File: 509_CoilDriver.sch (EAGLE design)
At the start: 230 parts, among them CN1 DF11-4DP-2DSA, CN10 826646-4, CN11 826646-4, CN12 BNC_ANGLE, CN13 BNC_ANGLE, CN14 BNC_ANGLE, CN15 DF11-4DP-2DSA, CN16 PCS-XE50LFD, CN17 PCS-XE50LFD, CN18 PH-2X5S, CN19 PIN_HEADER_SOCKET_14PIN, CN2 DF11-4DP-2DSA, CN20 DF11-14DP-2DSA, CN3 DF11-4DP-2DSA, CN4 DF11-4DP-2DSA, CN5 DF11-4DP-2DSA, CN6 DF11-4DP-2DSA, CN7 DF11-14DP-2DSA, CN8 PH-2X4S, CN9 DF11-4DP-2DSA, M1 VAB-3-10, M2 VAB-3-10, M3 VAB-3-10, SW1 A-12AV, SW2 A-12AV, SW3 A-12AV, SW4 A-12AV, U1 OPA2344EA, U10 74VHC4052AFT, U11 AD8227ARZ, U12 MAX4617CUE+, U13 MAX4617CUE+, U14 MAX4617CUE+, U15 MAX4617CUE+, U16 MAX4617CUE+, U17 MAX4617CUE+, U18 MAX4617CUE+, U19 MAX4617CUE+, U2 OPA2344EA, U20 MAX4617CUE+, U21 MAX4617CUE+, U22 MAX4617CUE+, U23 MAX4617CUE+, U24 MAX4617CUE+, U25 MAX4617CUE+, U26 TPS79933DDC, U27 5M160ZT100, U28 TPS79918DDC, U29 74VHC9541FT, U3 TS5A23159DGS, U30 TLP291GR, U4 TPS79933DDC, U5 OPA2344EA, U6 TPS3808G01DBV, U7 NJU7108F3, U8 OPA2344EA, U9 TS5A23159DGS

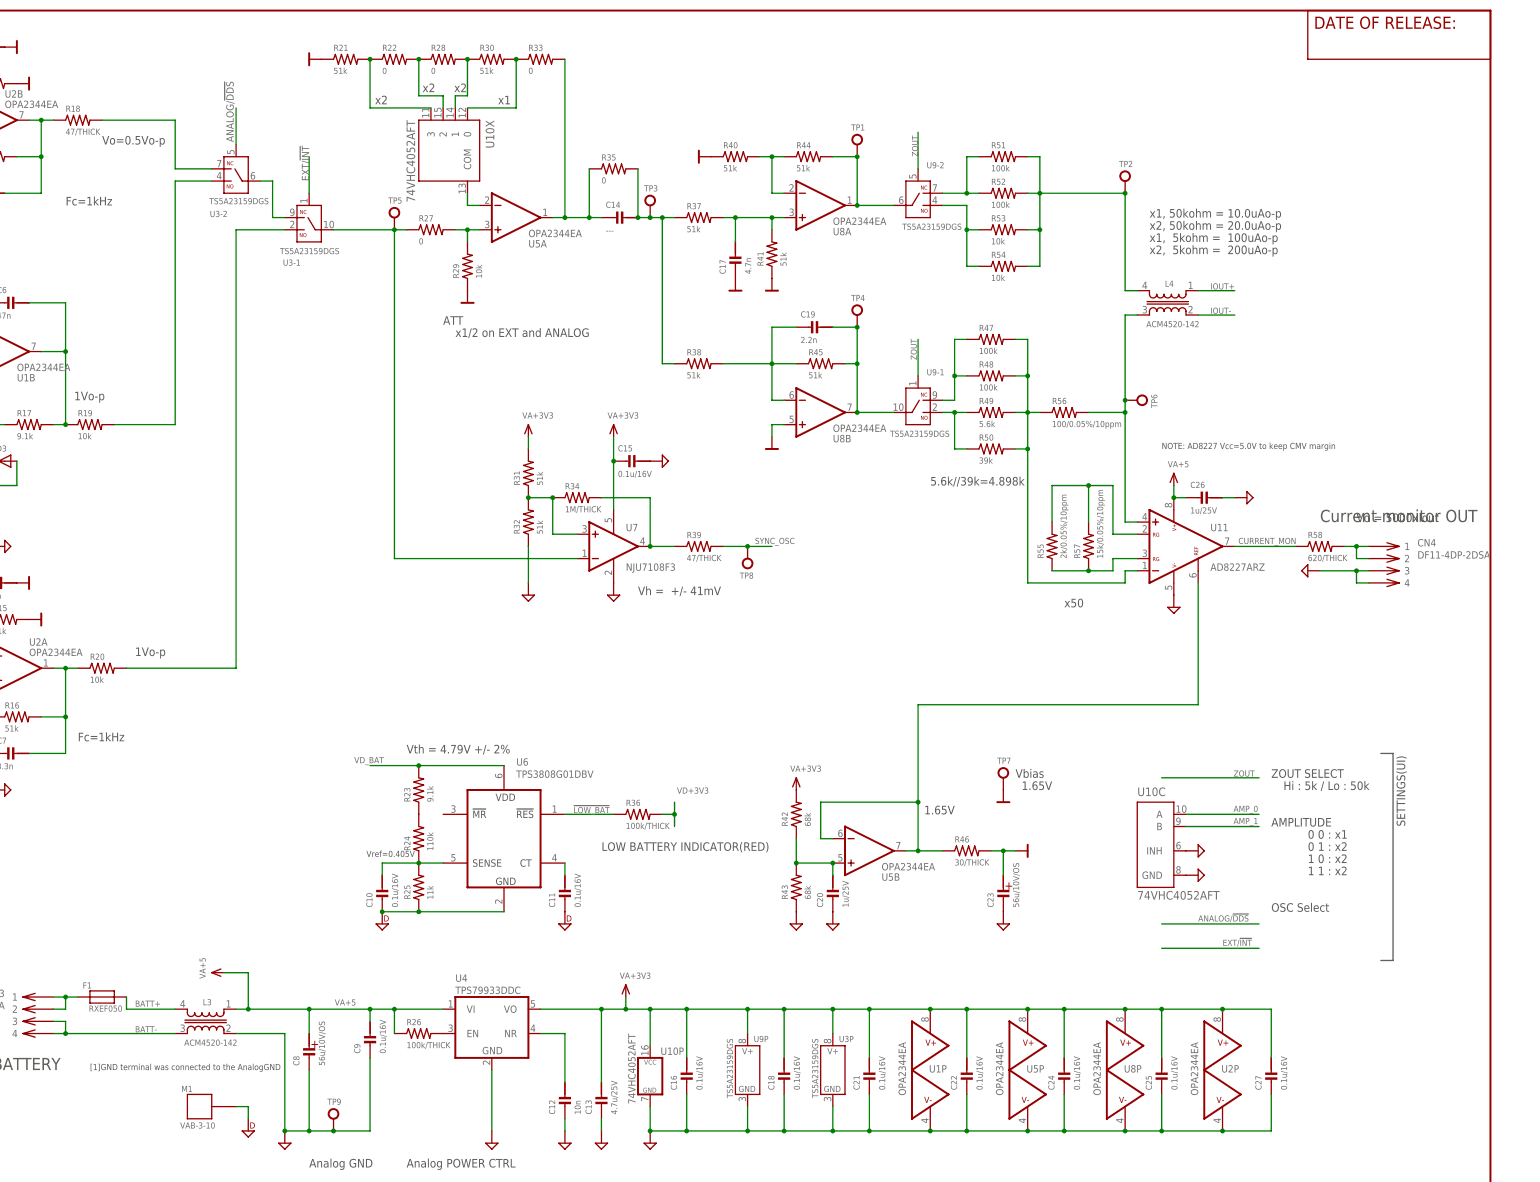
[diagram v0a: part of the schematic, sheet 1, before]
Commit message: modify Zout and Output Op-amps
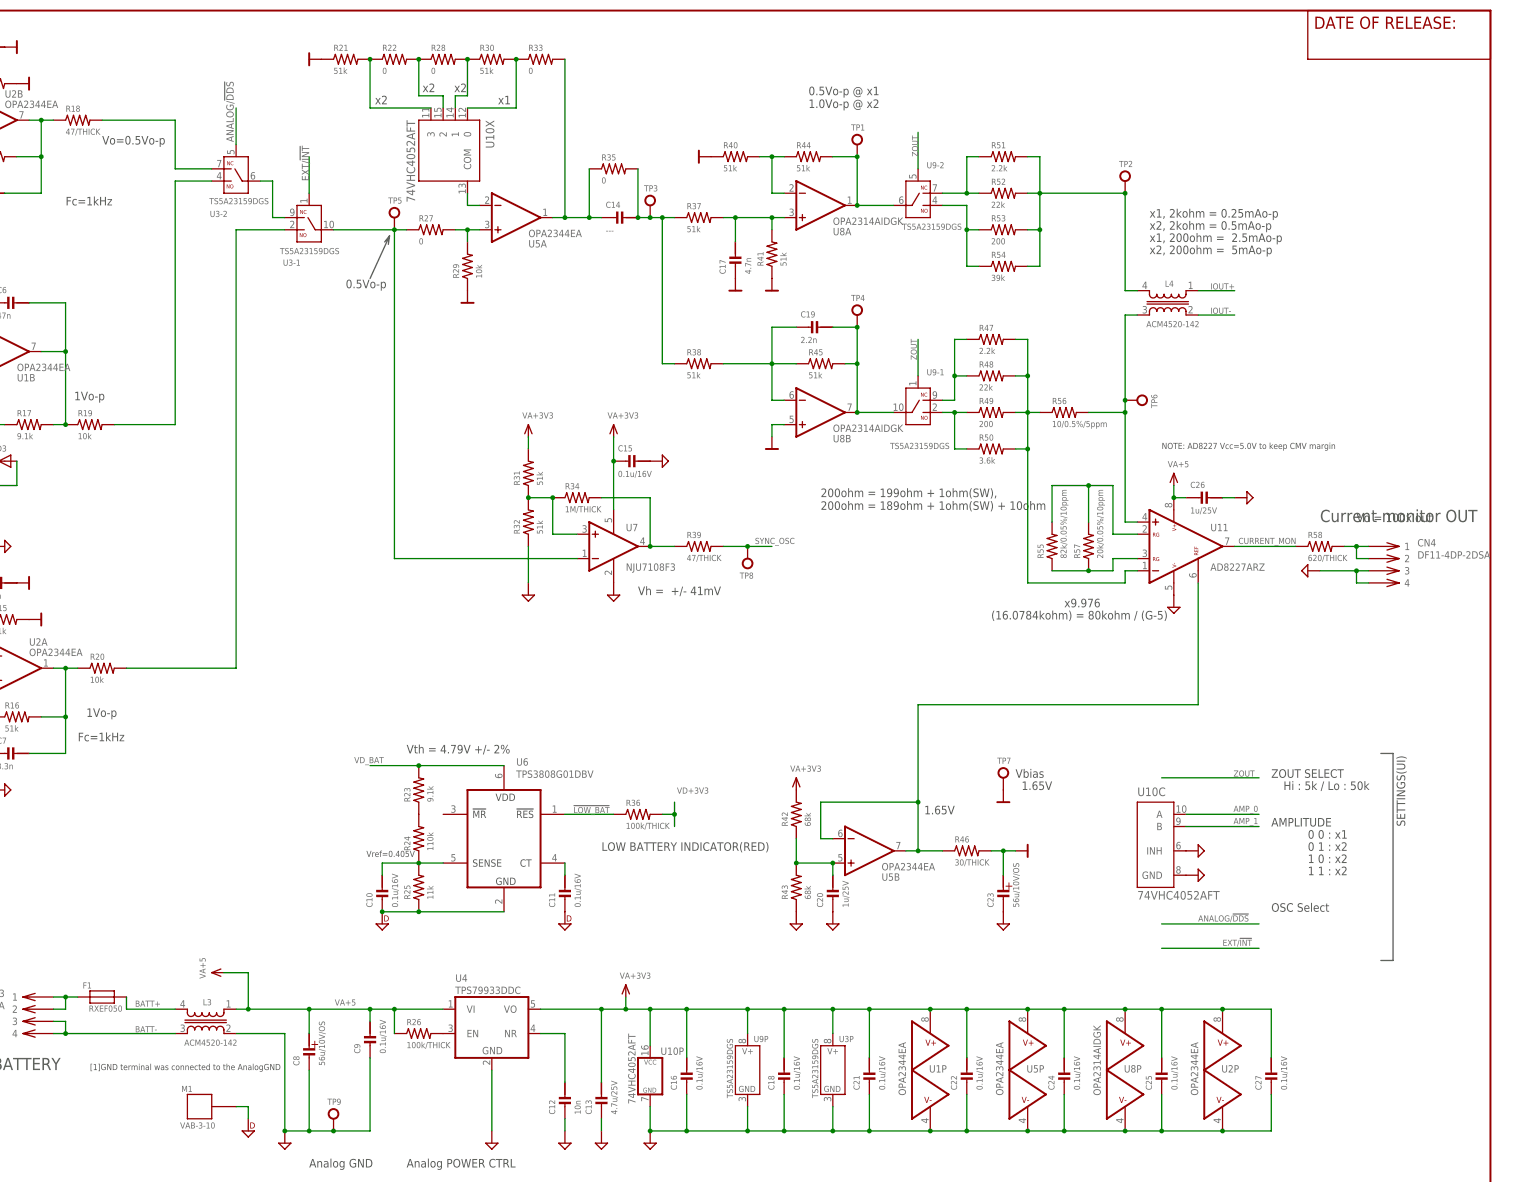
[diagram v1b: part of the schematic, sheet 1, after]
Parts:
- R47, R51: value 100k -> 2.2k
- R48, R52: value 100k -> 22k
- R49: value 5.6k -> 200
- R50: value 39k -> 3.6k
- R53: value 10k -> 200
- R54: value 10k -> 39k
- R55: value 2k/0.05%/10ppm -> 82k/0.05%/10ppm
- R56: value 100/0.05%/10ppm -> 10/0.5%/5ppm
- R57: value 15k/0.05%/10ppm -> 20k/0.05%/10ppm
- U8: value OPA2344EA -> OPA2314AIDGK
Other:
- note added: "(16.0784kohm) = 80kohm / (G-5)"
- note added: "0.5Vo-p"
- note added: "0.5Vo-p @ x1 1.0Vo-p @ x2"
- note added: "200ohm = 199ohm + 1ohm(SW), 200ohm = 189ohm + 1ohm(SW) + 10ohm"
- note added: "Vo = 100xIout"
- note added: "x1, 200ohm = 2.5mAo-p"
- note added: "x1, 2kohm = 0.25mAo-p"
- note added: "x2, 200ohm = 5mAo-p"
- note added: "x2, 2kohm = 0.5mAo-p"
- note added: "x9.976"
- note removed: "5.6k//39k=4.898k"
- note removed: "ATT"
- note removed: "Vo = 5000xIout"
- note removed: "x1, 50kohm = 10.0uAo-p"
- note removed: "x1, 5kohm = 100uAo-p"
- note removed: "x1/2 on EXT and ANALOG"
- note removed: "x2, 50kohm = 20.0uAo-p"
- note removed: "x2, 5kohm = 200uAo-p"
- note removed: "x50"
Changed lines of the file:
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@@
 <part name="U1" library="AEL_linear" deviceset="OPA2344" device="EA"/>
 <part name="U5" library="AEL_linear" deviceset="OPA2344" device="EA"/>
-<part name="U8" library="AEL_linear" deviceset="OPA2344" device="EA"/>
+<part name="U8" library="AEL_linear" deviceset="OPA2344" device="EA" value="OPA2314AIDGK"/>
 <part name="U9" library="AEL_linear" deviceset="TS5A23159" device="DGS"/>
 <part name="U10" library="AEL_CMOS_LOG" deviceset="74*4052" device="AFT" technology="VHC"/>
@@
 <part name="C17" library="AEL_RLC" deviceset="C" device="SMD2.0X1.2MM" value="4.7n"/>
 <part name="C19" library="AEL_RLC" deviceset="C" device="SMD2.0X1.2MM" value="2.2n"/>
-<part name="R52" library="AEL_RLC" deviceset="R" device="SMD1.6X0.8MM" value="100k"/>
-<part name="R53" library="AEL_RLC" deviceset="R" device="SMD1.6X0.8MM" value="10k"/>
-<part name="R48" library="AEL_RLC" deviceset="R" device="SMD1.6X0.8MM" value="100k"/>
-<part name="R49" library="AEL_RLC" deviceset="R" device="SMD1.6X0.8MM" value="5.6k"/>
+<part name="R52" library="AEL_RLC" deviceset="R" device="SMD1.6X0.8MM" value="22k"/>
+<part name="R53" library="AEL_RLC" deviceset="R" device="SMD1.6X0.8MM" value="200"/>
+<part name="R48" library="AEL_RLC" deviceset="R" device="SMD1.6X0.8MM" value="22k"/>
+<part name="R49" library="AEL_RLC" deviceset="R" device="SMD1.6X0.8MM" value="200"/>
 <part name="R31" library="AEL_RLC" deviceset="R" device="SMD1.6X0.8MM" value="51k"/>
 <part name="R34" library="AEL_RLC" deviceset="R" device="SMD1.6X0.8MM" value="1M/THICK"/>
@@
 <part name="PS6" library="AEL_powerline" deviceset="VA+3V3" device=""/>
 <part name="PS3" library="AEL_powerline" deviceset="VA+5" device=""/>
-<part name="R56" library="AEL_RLC" deviceset="R" device="SMD1.6X0.8MM" value="100/0.05%/10ppm"/>
+<part name="R56" library="AEL_RLC" deviceset="R" device="SMD1.6X0.8MM" value="10/0.5%/5ppm"/>
 <part name="U11" library="AEL_linear" deviceset="AD8227" device="RZ" technology="A"/>
-<part name="R57" library="AEL_RLC" deviceset="R" device="SMD1.6X0.8MM" value="15k/0.05%/10ppm"/>
-<part name="R55" library="AEL_RLC" deviceset="R" device="SMD1.6X0.8MM" value="2k/0.05%/10ppm"/>
+<part name="R57" library="AEL_RLC" deviceset="R" device="SMD1.6X0.8MM" value="20k/0.05%/10ppm"/>
+<part name="R55" library="AEL_RLC" deviceset="R" device="SMD1.6X0.8MM" value="82k/0.05%/10ppm"/>
 <part name="C26" library="AEL_RLC" deviceset="C" device="SMD1.6X0.8MM" value="1u/25V"/>
 <part name="V37" library="AEL_powerline" deviceset="AGND" device=""/>
@@
 <part name="V49" library="AEL_powerline" deviceset="DGND" device=""/>
 <part name="V48" library="AEL_powerline" deviceset="DGND" device=""/>
-<part name="R51" library="AEL_RLC" deviceset="R" device="SMD1.6X0.8MM" value="100k"/>
-<part name="R54" library="AEL_RLC" deviceset="R" device="SMD1.6X0.8MM" value="10k"/>
-<part name="R47" library="AEL_RLC" deviceset="R" device="SMD1.6X0.8MM" value="100k"/>
-<part name="R50" library="AEL_RLC" deviceset="R" device="SMD1.6X0.8MM" value="39k"/>
+<part name="R51" library="AEL_RLC" deviceset="R" device="SMD1.6X0.8MM" value="2.2k"/>
+<part name="R54" library="AEL_RLC" deviceset="R" device="SMD1.6X0.8MM" value="39k"/>
+<part name="R47" library="AEL_RLC" deviceset="R" device="SMD1.6X0.8MM" value="2.2k"/>
+<part name="R50" library="AEL_RLC" deviceset="R" device="SMD1.6X0.8MM" value="3.6k"/>
 <part name="V46" library="AEL_powerline" deviceset="DGND" device=""/>
 <part name="V45" library="AEL_powerline" deviceset="DGND" device=""/>
@@
 <text x="290.83" y="116.84" size="1.778" layer="97">1.65V</text>
 <text x="48.26" y="182.88" size="1.778" layer="97">Fo: +/-6% ADJ</text>
-<text x="317.5" y="236.22" size="1.778" layer="97" font="fixed">x1, 50kohm = 10.0uAo-p</text>
-<text x="317.5" y="233.68" size="1.778" layer="97" font="fixed">x2, 50kohm = 20.0uAo-p</text>
-<text x="317.5" y="231.14" size="1.778" layer="97" font="fixed">x1,  5kohm =  100uAo-p</text>
-<text x="317.5" y="228.6" size="1.778" layer="97" font="fixed">x2,  5kohm =  200uAo-p</text>
-<text x="172.72" y="211.328" size="1.778" layer="97">x1/2 on EXT and ANALOG</text>
-<text x="299.72" y="154.94" size="1.778" layer="97">x50</text>
+<text x="317.5" y="236.22" size="1.778" layer="97" font="fixed">x1, 2kohm = 0.25mAo-p</text>
+<text x="317.5" y="233.68" size="1.778" layer="97" font="fixed">x2, 2kohm = 0.5mAo-p</text>
+<text x="317.5" y="231.14" size="1.778" layer="97" font="fixed">x1, 200ohm =  2.5mAo-p</text>
+<text x="317.5" y="228.6" size="1.778" layer="97" font="fixed">x2, 200ohm =  5mAo-p</text>
+<text x="149.86" y="221.488" size="1.778" layer="97">0.5Vo-p</text>
+<text x="299.72" y="154.94" size="1.778" layer="97">x9.976</text>
 <text x="20.32" y="264.16" size="1.778" layer="97">DDS Input (diff)</text>
 <text x="30.48" y="259.08" size="1.778" layer="97">+</text>
@@
 <text x="99.06" y="251.46" size="1.778" layer="97">Vo=0.5Vo-p</text>
 <text x="91.44" y="238.76" size="1.778" layer="97">Fc=1kHz</text>
-<text x="170.18" y="213.868" size="1.778" layer="97">ATT</text>
 <text x="96.52" y="58.42" size="1.27" layer="97">[1]GND terminal was connected to the AnalogGND</text>
 <text x="76.2" y="58.42" size="2.54" layer="97">BATTERY</text>
@@
 <text x="320.04" y="187.96" size="1.27" layer="97">NOTE: AD8227 Vcc=5.0V to keep CMV margin</text>
 <text x="93.98" y="127" size="1.778" layer="97">Fc=1kHz</text>
-<text x="360.68" y="172.72" size="1.778" layer="97">Vo = 5000xIout</text>
+<text x="360.68" y="172.72" size="1.778" layer="97">Vo = 100xIout</text>
 <text x="22.86" y="233.68" size="1.778" layer="97">Iout FS =2.5mA, Zout = 200ohm
  -&gt; Vout(diff) = 0.5Vp-p
@@
  -&gt; Vout(SE) = 1Vp-p =0.5Vo-p</text>
 <text x="93.218" y="198.12" size="1.778" layer="97">1Vo-p</text>
-<text x="105.918" y="144.78" size="1.778" layer="97">1Vo-p</text>
+<text x="95.758" y="132.08" size="1.778" layer="97">1Vo-p</text>
 <text x="20.32" y="149.86" size="1.778" layer="97">EXT OSC Input (SE)</text>
 <text x="22.098" y="129.54" size="1.778" layer="97">+/-1V + 1.65Vdc
 0.1Hz - 100Hz</text>
 <text x="342.9" y="91.44" size="1.778" layer="97">OSC Select</text>
-<text x="271.78" y="180.34" size="1.778" layer="97">5.6k//39k=4.898k</text>
+<text x="248.92" y="175.26" size="1.778" layer="97">200ohm = 199ohm + 1ohm(SW),
+200ohm = 189ohm + 1ohm(SW) + 10ohm</text>
 <wire x1="365.76" y1="124.46" x2="368.3" y2="124.46" width="0.1524" layer="97"/>
 <wire x1="368.3" y1="124.46" x2="368.3" y2="81.28" width="0.1524" layer="97"/>
@@
 <text x="370.84" y="109.22" size="1.778" layer="97" rot="R90">SETTINGS(UI)</text>
 <text x="60.96" y="223.52" size="1.778" layer="97">&gt;ASSEMBLY_VARIANT </text>
+<text x="246.38" y="259.08" size="1.778" layer="97" font="fixed">0.5Vo-p @ x1
+1.0Vo-p @ x2</text>
+<text x="284.48" y="152.4" size="1.778" layer="97">(16.0784kohm) = 80kohm / (G-5)</text>
+<wire x1="154.94" y1="223.52" x2="159.004" y2="232.41" width="0.1524" layer="97"/>
+<wire x1="159.004" y1="232.41" x2="158.75" y2="230.632" width="0.1524" layer="97"/>
+<wire x1="159.004" y1="232.41" x2="157.988" y2="231.14" width="0.1524" layer="97"/>
 </plain>
 <instances>
@@
 <instance part="U9" gate="-1" x="269.24" y="195.58" smashed="yes">
 <attribute name="NAME" x="271.018" y="203.327" size="1.27" layer="95"/>
-<attribute name="VALUE" x="263.398" y="190.5" size="1.27" layer="96"/>
+<attribute name="VALUE" x="263.398" y="187.96" size="1.27" layer="96"/>
 </instance>
 <instance part="U9" gate="-2" x="269.24" y="238.76" smashed="yes">
